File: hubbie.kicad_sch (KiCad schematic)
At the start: 70 parts, among them J1 USB_B_Micro, J10 MotorAL, J11 MotorAR, J12 SERVO_0, J13 SERVO_1, J14 DEBUG, J15 AIR_SENSOR, J16 RST_BTN, J17 SERIAL, J18 ActionBtn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

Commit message: Updated ultrasonic sensor vcc to 5v
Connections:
- net +3.3V: no longer J5.1 (Pin_1), J6.1 (Pin_1), J7.1 (Pin_1)
- net VBUS: now also J5.1 (Pin_1), J6.1 (Pin_1), J7.1 (Pin_1)
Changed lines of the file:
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@@
   (junction (at 75.184 207.772) (diameter 0) (color 0 0 0 0)
   )
-  (junction (at 170.815 214.63) (diameter 0) (color 0 0 0 0)
-  )
   (junction (at 283.21 66.04) (diameter 0) (color 0 0 0 0)
   )
@@
     (stroke (width 0) (type default))
   )
+  (wire (pts (xy 168.91 214.63) (xy 173.99 214.63))
+    (stroke (width 0) (type default))
+  )
   (wire (pts (xy 183.134 38.354) (xy 183.134 40.64))
     (stroke (width 0) (type default))
@@
     (stroke (width 0) (type default))
   )
-  (wire (pts (xy 170.815 214.63) (xy 173.99 214.63))
-    (stroke (width 0) (type default))
-  )
   (wire (pts (xy 303.53 93.98) (xy 303.276 93.98))
     (stroke (width 0) (type default))
@@
     (stroke (width 0) (type default))
   )
-  (wire (pts (xy 170.688 214.63) (xy 170.815 214.63))
-    (stroke (width 0) (type default))
-  )
   (wire (pts (xy 52.578 134.62) (xy 63.5 134.62))
     (stroke (width 0) (type default))
@@
     (effects (font (size 1.27 1.27)) (justify right bottom))
   )
+  (symbol (lib_id "power:VBUS") (at 170.815 226.695 90) (unit 1)
+    (in_bom yes) (on_board yes) (dnp no)
+    (property "Reference" "#PWR03" (at 174.625 226.695 0)
+      (effects (font (size 1.27 1.27)) hide)
+    )
+    (property "Value" "VBUS" (at 168.275 226.695 90)
+      (effects (font (size 1.27 1.27)) (justify left))
+    )
+    (property "Footprint" "" (at 170.815 226.695 0)
+      (effects (font (size 1.27 1.27)) hide)
+    )
+    (property "Datasheet" "" (at 170.815 226.695 0)
+      (effects (font (size 1.27 1.27)) hide)
+    )
+    (pin "1")
+    (instances
+      (project "hubbie"
+        (path "/4b079591-78aa-460a-b818-67c079ee5725"
+          (reference "#PWR03") (unit 1)
+        )
+      )
+    )
+  )
   (symbol (lib_id "power:GND") (at 278.13 157.48 0) (unit 1)
     (in_bom yes) (on_board yes) (dnp no) (fields_autoplaced)
@@
     )
   )
+  (symbol (lib_id "power:VBUS") (at 168.91 214.63 90) (unit 1)
+    (in_bom yes) (on_board yes) (dnp no)
+    (property "Reference" "#PWR02" (at 172.72 214.63 0)
+      (effects (font (size 1.27 1.27)) hide)
+    )
+    (property "Value" "VBUS" (at 166.37 214.63 90)
+      (effects (font (size 1.27 1.27)) (justify left))
+    )
+    (property "Footprint" "" (at 168.91 214.63 0)
+      (effects (font (size 1.27 1.27)) hide)
+    )
+    (property "Datasheet" "" (at 168.91 214.63 0)
+      (effects (font (size 1.27 1.27)) hide)
+    )
+    (pin "1")
+    (instances
+      (project "hubbie"
+        (path "/4b079591-78aa-460a-b818-67c079ee5725"
+          (reference "#PWR02") (unit 1)
+        )
+      )
+    )
+  )
   (symbol (lib_id "Mechanical:MountingHole") (at 382.27 80.01 0) (unit 1)
     (in_bom yes) (on_board yes) (dnp no) (fields_autoplaced)
@@
     )
   )
+  (symbol (lib_id "power:VBUS") (at 170.815 238.76 90) (unit 1)
+    (in_bom yes) (on_board yes) (dnp no)
+    (property "Reference" "#PWR04" (at 174.625 238.76 0)
+      (effects (font (size 1.27 1.27)) hide)
+    )
+    (property "Value" "VBUS" (at 168.275 238.76 90)
+      (effects (font (size 1.27 1.27)) (justify left))
+    )
+    (property "Footprint" "" (at 170.815 238.76 0)
+      (effects (font (size 1.27 1.27)) hide)
+    )
+    (property "Datasheet" "" (at 170.815 238.76 0)
+      (effects (font (size 1.27 1.27)) hide)
+    )
+    (pin "1")
+    (instances
+      (project "hubbie"
+        (path "/4b079591-78aa-460a-b818-67c079ee5725"
+          (reference "#PWR04") (unit 1)
+        )
+      )
+    )
+  )
   (symbol (lib_id "power:GND") (at 257.048 53.848 0) (unit 1)
     (in_bom yes) (on_board yes) (dnp no) (fields_autoplaced)
@@
     )
   )
-  (symbol (lib_id "power:+3.3V") (at 170.815 238.76 90) (unit 1)
-    (in_bom yes) (on_board yes) (dnp no) (fields_autoplaced)
-    (property "Reference" "#PWR04" (at 174.625 238.76 0)
-      (effects (font (size 1.27 1.27)) hide)
-    )
-    (property "Value" "+3.3V" (at 167.64 238.7599 90)
-      (effects (font (size 1.27 1.27)) (justify left))
-    )
-    (property "Footprint" "" (at 170.815 238.76 0)
-      (effects (font (size 1.27 1.27)) hide)
-    )
-    (property "Datasheet" "" (at 170.815 238.76 0)
-      (effects (font (size 1.27 1.27)) hide)
-    )
-    (pin "1")
-    (instances
-      (project "hubbie"
-        (path "/4b079591-78aa-460a-b818-67c079ee5725"
-          (reference "#PWR04") (unit 1)
-        )
-      )
-    )
-  )
   (symbol (lib_id "Device:C") (at 313.944 45.974 0) (unit 1)
     (in_bom yes) (on_board yes) (dnp no)
@@
     )
   )
-  (symbol (lib_id "power:+3.3V") (at 170.815 226.695 90) (unit 1)
-    (in_bom yes) (on_board yes) (dnp no) (fields_autoplaced)
-    (property "Reference" "#PWR03" (at 174.625 226.695 0)
-      (effects (font (size 1.27 1.27)) hide)
-    )
-    (property "Value" "+3.3V" (at 167.64 226.6949 90)
-      (effects (font (size 1.27 1.27)) (justify left))
-    )
-    (property "Footprint" "" (at 170.815 226.695 0)
-      (effects (font (size 1.27 1.27)) hide)
-    )
-    (property "Datasheet" "" (at 170.815 226.695 0)
-      (effects (font (size 1.27 1.27)) hide)
-    )
-    (pin "1")
-    (instances
-      (project "hubbie"
-        (path "/4b079591-78aa-460a-b818-67c079ee5725"
-          (reference "#PWR03") (unit 1)
-        )
-      )
-    )
-  )
   (symbol (lib_id "Connector:Conn_01x03_Female") (at 210.312 61.722 0) (unit 1)
     (in_bom yes) (on_board yes) (dnp no) (fields_autoplaced)
@@
         )
       )
-    )
-  )
-  (symbol (lib_id "power:+3.3V") (at 170.815 214.63 90) (unit 1)
-    (in_bom yes) (on_board yes) (dnp no) (fields_autoplaced)
-    (property "Reference" "#PWR02" (at 174.625 214.63 0)
-      (effects (font (size 1.27 1.27)) hide)
-    )
-    (property "Value" "+3.3V" (at 167.64 214.6299 90)
-      (effects (font (size 1.27 1.27)) (justify left))
-    )
-    (property "Footprint" "" (at 170.815 214.63 0)
-      (effects (font (size 1.27 1.27)) hide)
-    )
-    (property "Datasheet" "" (at 170.815 214.63 0)
-      (effects (font (size 1.27 1.27)) hide)
-    )
-    (pin "1")
-    (instances
-      (project "hubbie"
-        (path "/4b079591-78aa-460a-b818-67c079ee5725"
-          (reference "#PWR02") (unit 1)
-        )
-      )

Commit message: Add usb c support and fix wrong voltage sources
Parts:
- removed J1: USB_B_Micro, Connector_USB:USB_Micro-B_Amphenol_10118194_Horizontal, symbol Connector:USB_B_Micro
- added J21: DHT22, Connector_JST:JST_XH_B3B-XH-A_1x03_P2.50mm_Vertical, symbol Connector_Generic:Conn_01x03
- added J22: USB_C_Receptacle_USB2.0, Connector_USB:USB_C_Receptacle_XKB_U262-16XN-4BVC11, symbol Connector:USB_C_Receptacle_USB2.0
- added R7, R8: 5.4k, Resistor_SMD:R_0603_1608Metric, symbol Device:R
- J15: footprint Connector_JST:JST_XH_B4B-XH-A_1x04_P2.50mm_Vertical -> Connector_JST:JST_XH_B5B-XH-AM_1x05_P2.50mm_Vertical
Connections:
- net +3.3V: now also J21.1 (Pin_1)
- net GND: now also J21.3 (Pin_3), J22.A1 (GND), J22.A12 (GND), J22.B1 (GND), J22.B12 (GND), J22.S1 (SHIELD), R7.2, R8.2
- net USB_D+: now also J22.A6 (D+), J22.B6 (D+)
- net USB_D-: now also J22.A7 (D-), J22.B7 (D-)
- net VBUS: now also J22.A4 (VBUS), J22.A9 (VBUS), J22.B4 (VBUS), J22.B9 (VBUS)
- net DHT: now reaches U5.41 (GPIO29_ADC3)
- net DHT: now also J21.2 (Pin_2)
- new net: J22.A5 (CC1), R7.1
- new net: J22.B5 (CC2), R8.1

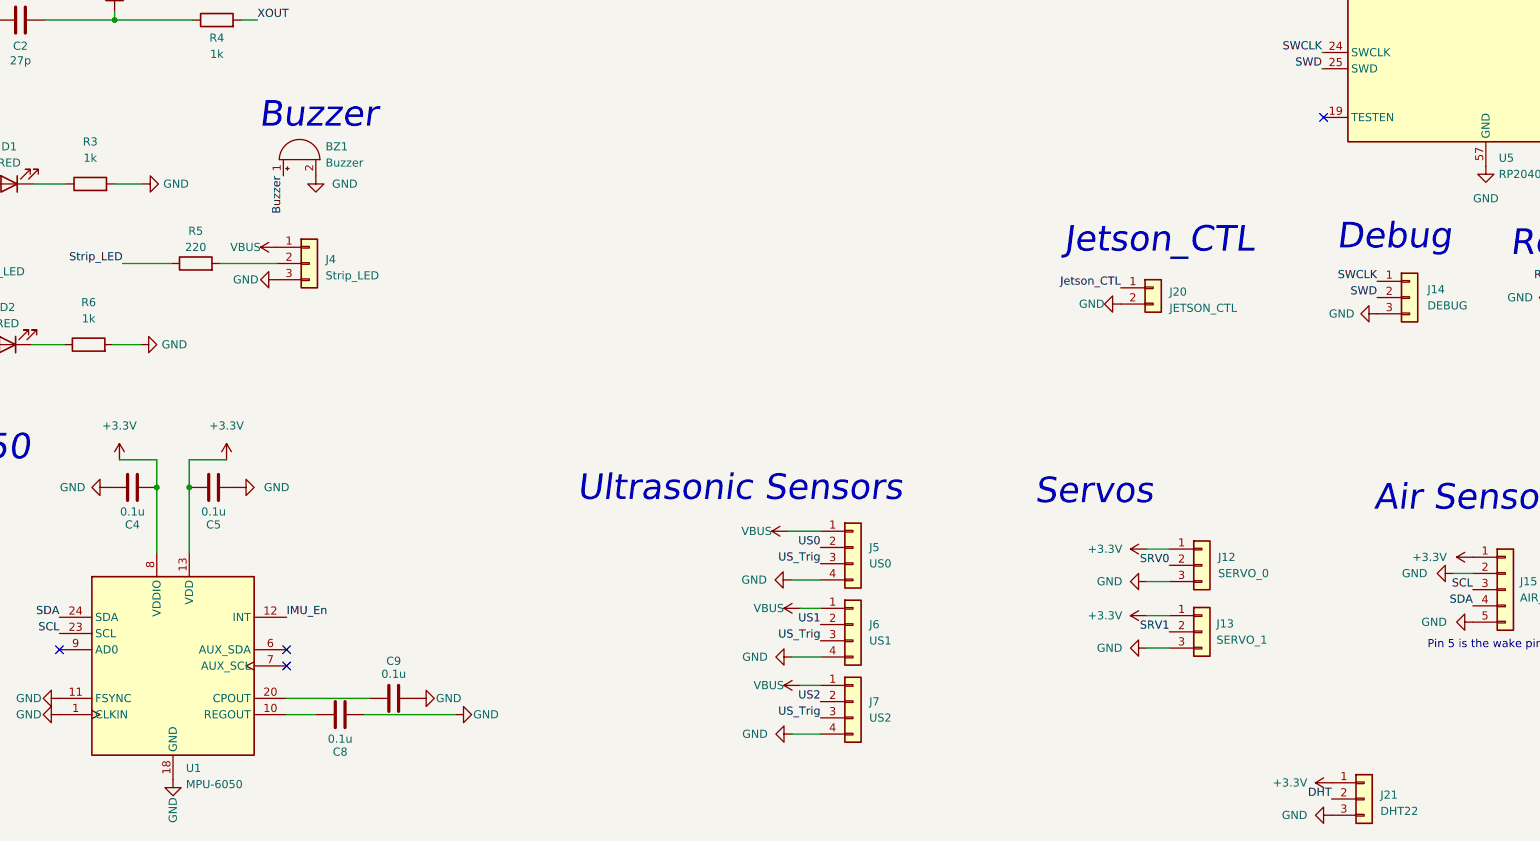
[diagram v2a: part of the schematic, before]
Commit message: Update wrong capacitor values (C4 and C9)
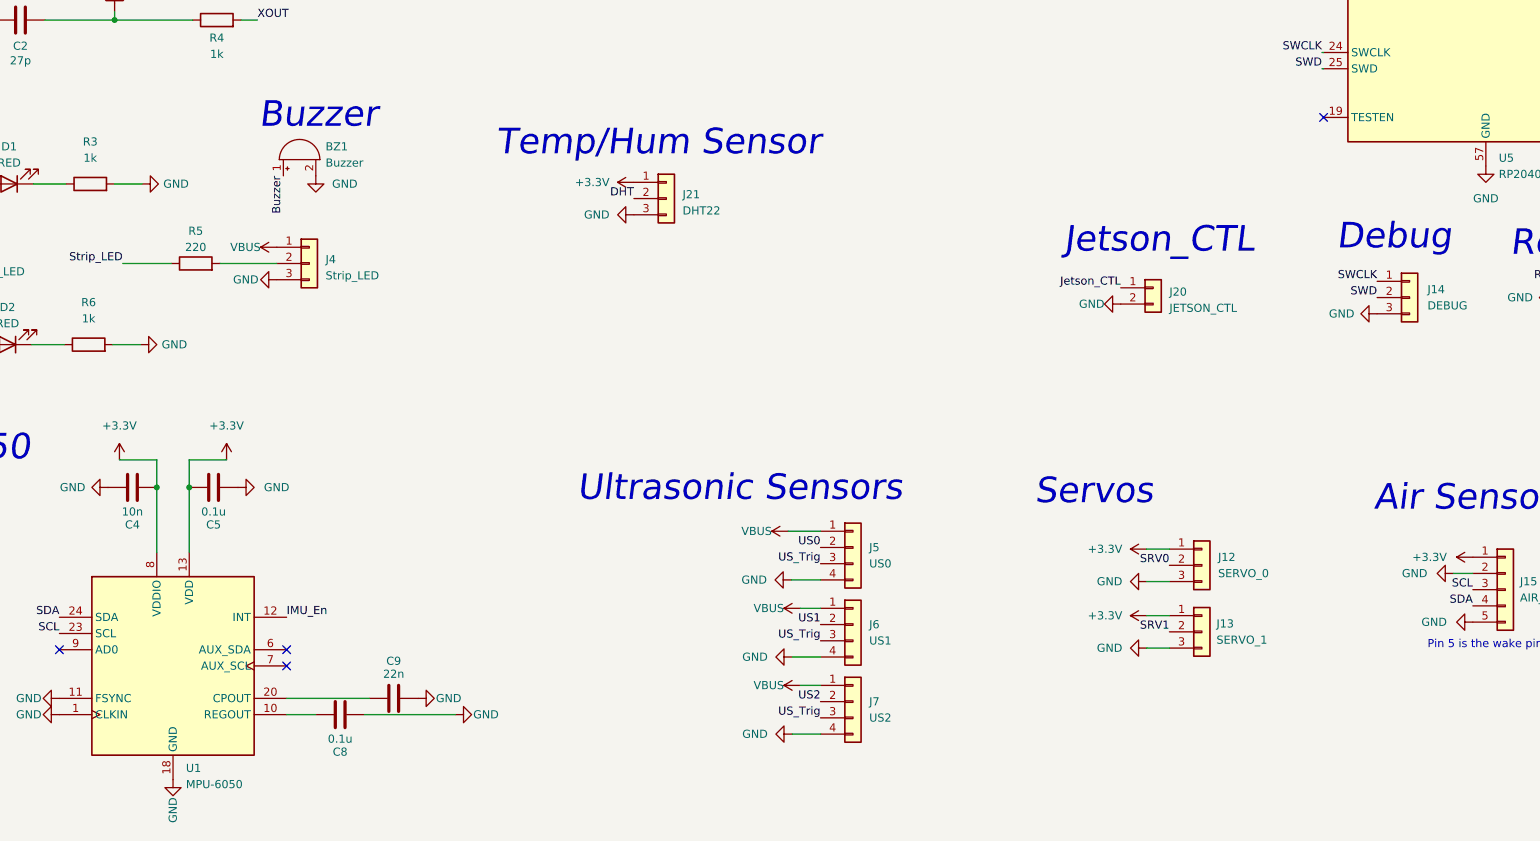
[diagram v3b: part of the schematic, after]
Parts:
- C4: value 0.1u -> 10n
- C9: value 0.1u -> 22n
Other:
- note added: "Temp/Hum Sensor"
- moved on the sheet: J21
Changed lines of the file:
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@@
     (effects (font (size 4 4) italic) (justify left bottom))
   )
+  (text "Temp/Hum Sensor" (at 123.19 156.21 0)
+    (effects (font (size 4 4) italic) (justify left bottom))
+  )
   (text "RP2040" (at 237.998 33.02 0)
     (effects (font (size 4 4) italic) (justify left bottom))
@@
     (effects (font (size 1.27 1.27)) (justify right bottom))
   )
-  (label "DHT" (at 254 256.54 180) (fields_autoplaced)
+  (label "DHT" (at 144.78 162.56 180) (fields_autoplaced)
     (effects (font (size 1.27 1.27)) (justify right bottom))
   )
@@
     )
   )
-  (symbol (lib_id "power:+3.3V") (at 254 254 90) (unit 1)
+  (symbol (lib_id "power:+3.3V") (at 144.78 160.02 90) (unit 1)
     (in_bom yes) (on_board yes) (dnp no) (fields_autoplaced)
-    (property "Reference" "#PWR015" (at 257.81 254 0)
+    (property "Reference" "#PWR015" (at 148.59 160.02 0)
       (effects (font (size 1.27 1.27)) hide)
     )
-    (property "Value" "+3.3V" (at 250.19 253.9999 90)
+    (property "Value" "+3.3V" (at 140.97 160.0199 90)
       (effects (font (size 1.27 1.27)) (justify left))
     )
-    (property "Footprint" "" (at 254 254 0)
+    (property "Footprint" "" (at 144.78 160.02 0)
       (effects (font (size 1.27 1.27)) hide)
     )
-    (property "Datasheet" "" (at 254 254 0)
+    (property "Datasheet" "" (at 144.78 160.02 0)
       (effects (font (size 1.27 1.27)) hide)
     )
@@
       (effects (font (size 1.27 1.27)))
     )
-    (property "Value" "0.1u" (at 107.188 236.982 90)
+    (property "Value" "22n" (at 107.188 236.982 90)
       (effects (font (size 1.27 1.27)))
     )
@@
     )
   )
-  (symbol (lib_id "Connector_Generic:Conn_01x03") (at 259.08 256.54 0) (unit 1)
+  (symbol (lib_id "Connector_Generic:Conn_01x03") (at 149.86 162.56 0) (unit 1)
     (in_bom yes) (on_board yes) (dnp no) (fields_autoplaced)
-    (property "Reference" "J21" (at 261.62 255.905 0)
+    (property "Reference" "J21" (at 152.4 161.925 0)
       (effects (font (size 1.27 1.27)) (justify left))
     )
-    (property "Value" "DHT22" (at 261.62 258.445 0)
+    (property "Value" "DHT22" (at 152.4 164.465 0)
       (effects (font (size 1.27 1.27)) (justify left))
     )
-    (property "Footprint" "Connector_JST:JST_XH_B3B-XH-A_1x03_P2.50mm_Vertical" (at 259.08 256.54 0)
+    (property "Footprint" "Connector_JST:JST_XH_B3B-XH-A_1x03_P2.50mm_Vertical" (at 149.86 162.56 0)
       (effects (font (size 1.27 1.27)) hide)
     )
-    (property "Datasheet" "~" (at 259.08 256.54 0)
+    (property "Datasheet" "~" (at 149.86 162.56 0)
       (effects (font (size 1.27 1.27)) hide)
     )
@@
     )
   )
-  (symbol (lib_id "power:GND") (at 254 259.08 270) (unit 1)
+  (symbol (lib_id "power:GND") (at 144.78 165.1 270) (unit 1)
     (in_bom yes) (on_board yes) (dnp no) (fields_autoplaced)
-    (property "Reference" "#PWR016" (at 247.65 259.08 0)
+    (property "Reference" "#PWR016" (at 138.43 165.1 0)
       (effects (font (size 1.27 1.27)) hide)
     )
-    (property "Value" "GND" (at 250.19 259.0799 90)
+    (property "Value" "GND" (at 140.97 165.0999 90)
       (effects (font (size 1.27 1.27)) (justify right))
     )
-    (property "Footprint" "" (at 254 259.08 0)
+    (property "Footprint" "" (at 144.78 165.1 0)
       (effects (font (size 1.27 1.27)) hide)
     )
-    (property "Datasheet" "" (at 254 259.08 0)
+    (property "Datasheet" "" (at 144.78 165.1 0)
       (effects (font (size 1.27 1.27)) hide)
     )
@@
       (effects (font (size 1.27 1.27)))
     )
-    (property "Value" "0.1u" (at 66.294 211.582 90)
+    (property "Value" "10n" (at 66.294 211.582 90)
       (effects (font (size 1.27 1.27)))
     )
